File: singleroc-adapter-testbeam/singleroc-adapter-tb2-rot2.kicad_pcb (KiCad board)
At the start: 2 copper layers, 64 x 50.8 mm, 34 parts

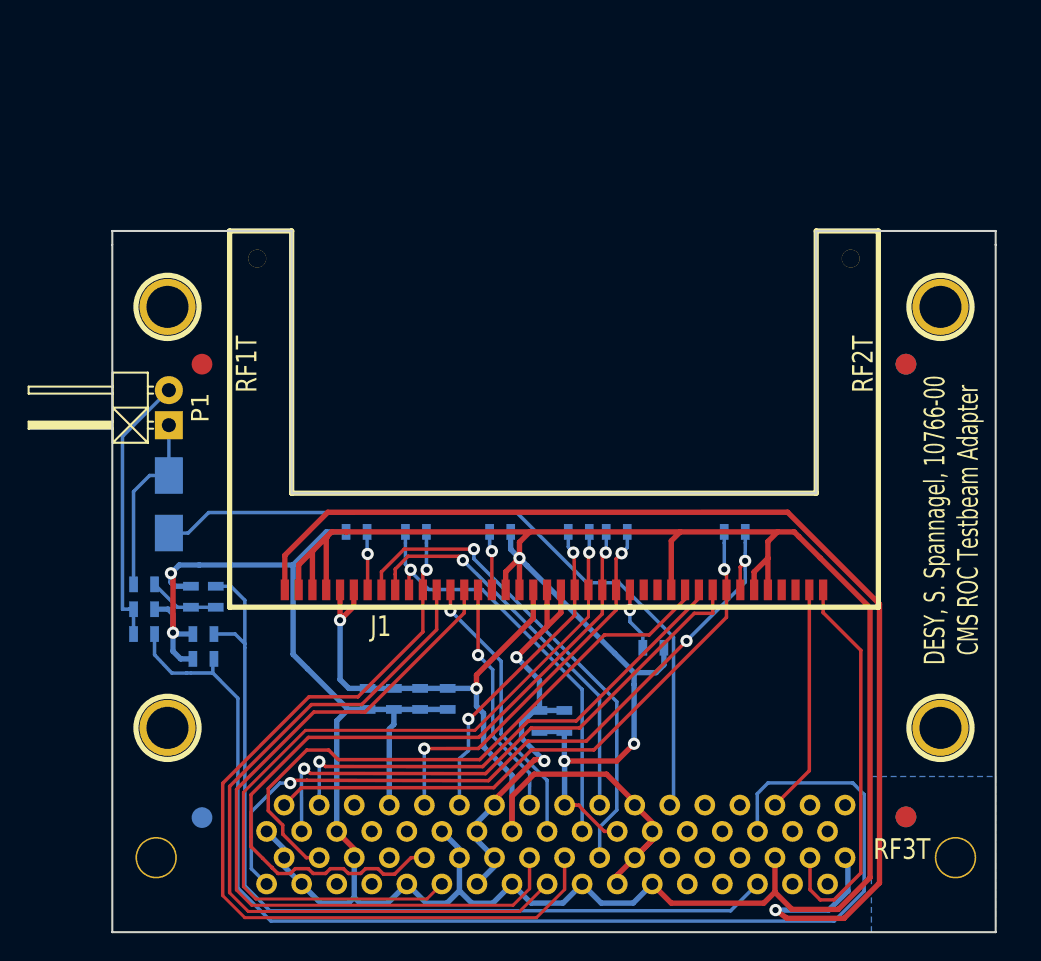
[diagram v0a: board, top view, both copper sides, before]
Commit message: Basic formfactor defined. Hispeed signals: changed resistor footprints to 0402 to save some space.
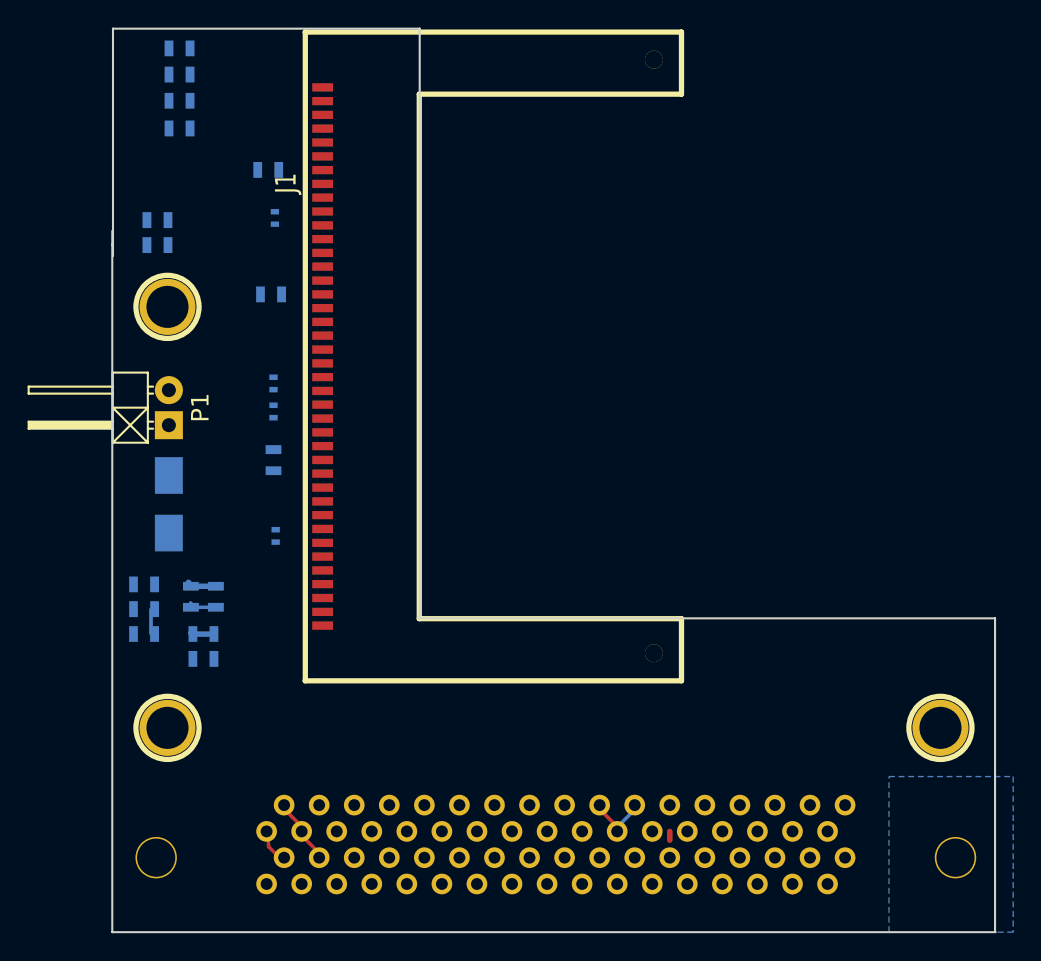
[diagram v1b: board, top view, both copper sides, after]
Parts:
- removed the ? at (147.0, 73.5)
- removed RF1B, RF1T, RF2B, RF2T, RF3B, RF3T: , Connect:1pin
- R1, R2, R3, R4: footprint SMD0603-new:SM0603 -> Resistors_SMD:R_0402
- moved C5 49.1 mm to (91.9, 54.8), turned to 180 degrees
- moved C7 47.8 mm to (91.9, 56.7), turned to 180 degrees
- moved C8 46.7 mm to (91.9, 58.6), turned to 180 degrees
- moved C9 45.7 mm to (91.9, 60.6), turned to 180 degrees
- moved C4 45.6 mm to (90.3, 67.2), turned to 180 degrees
- moved C6 45.4 mm to (90.3, 69.0), turned to 180 degrees
- moved R4 33.3 mm to (98.8, 90.1), turned to 90 degrees
- moved C3 30.7 mm to (98.7, 84.6), turned to 90 degrees
- moved C1 27.0 mm to (98.3, 63.6)
- moved R2 26.4 mm to (98.7, 81.1), turned to 90 degrees
- moved R1 24.9 mm to (98.8, 67.1), turned to 90 degrees
- moved R3 24.6 mm to (98.7, 79.0), turned to 90 degrees
- moved C2 23.9 mm to (98.5, 72.6), turned to 0 degrees
- moved J1 23.8 mm to (102.2, 77.1), turned to 270 degrees
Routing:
- net GND: track 263.5 -> 8.50 mm, vias 5 -> 0
- net AIN0: track 89.1 -> 0.00 mm
- net HV: track 87.1 -> 0.00 mm, vias 1 -> 0
- net AIN1: track 64.4 -> 0.00 mm
- net I2C_DAT+: track 63.1 -> 0.00 mm, vias 1 -> 0
- net VD: track 62.5 -> 0.00 mm, vias 2 -> 0
- net CLK+: track 58.5 -> 0.00 mm, vias 1 -> 0
- net CTR-: track 55.5 -> 0.00 mm, vias 1 -> 0
- net I2C_A2: track 55.2 -> 0.00 mm
- net I2C_A0: track 54.7 -> 0.00 mm
- net TIN+: track 54.3 -> 0.00 mm, vias 3 -> 0
- net Net-(F1-Pad2): track 53.2 -> 0.00 mm
- net SOUT-: track 44.2 -> 0.00 mm
- net TIN-: track 43.9 -> 1.48 mm, vias 1 -> 0
- net RESET: track 40.9 -> 3.06 mm, vias 1 -> 0
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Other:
- board size 64 x 50.8 mm -> 64 x 65.5 mm
- board text removed: "DESY, S. Spannagel, 10766-00 CMS ROC Testbeam Adapter"

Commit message: Proceeding...
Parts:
- C1, C10, C11, C2, C3, C4, C5, C6, C7, C8, C9, F1, R1, R2, R3, R4, R5, R6, R7, R8, R9: moved to F.Cu
- moved F1 11.9 mm to (98.1, 97.4), turned to 90 degrees
- moved R8 9.43 mm to (93.3, 86.8)
- moved R5 9.11 mm to (93.3, 89.0)
- moved C11 7.69 mm to (93.3, 91.3)
- moved R7 6.33 mm to (90.3, 87.4), turned to 270 degrees
- moved R9 2.33 mm to (90.4, 94.8), turned to 270 degrees
- moved C10 2.25 mm to (91.8, 98.5)
- moved R3 1.80 mm to (96.9, 79.1)
- moved R2 1.80 mm to (96.9, 81.1)
- moved R4 1.78 mm to (97.1, 90.0)
- moved R6 1.77 mm to (92.8, 94.8), turned to 90 degrees
- moved C3 1.41 mm to (97.5, 83.8), turned to 0 degrees
- moved C5 1.40 mm to (91.0, 55.9)
- moved C7 1.40 mm to (91.0, 57.8)
- moved C8 1.40 mm to (91.0, 59.7)
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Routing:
- net HV: track 0.00 -> 98.3 mm, vias 0 -> 1
- net TOUT-: track 0.00 -> 70.1 mm, vias 0 -> 1
- net I2C_DAT+: track 0.00 -> 69.6 mm, vias 0 -> 1
- net GND: track 8.50 -> 77.2 mm, vias 0 -> 18
- net I2C_DAT-: track 0.00 -> 67.6 mm, vias 0 -> 1
- net VD: track 0.00 -> 67.5 mm, vias 0 -> 7
- net I2C_A0: track 0.00 -> 62.0 mm
- net TOUT+: track 2.91 -> 64.8 mm, vias 0 -> 1
- net VA: track 0.00 -> 61.8 mm, vias 0 -> 4
- net I2C_A1: track 0.00 -> 54.1 mm
- net CLK+: track 0.00 -> 52.2 mm, vias 0 -> 2
- net I2C_A2: track 0.00 -> 51.8 mm
- net CLK-: track 0.00 -> 46.6 mm, vias 0 -> 1
- net I2C_A3: track 0.00 -> 46.1 mm
- net CTR-: track 0.00 -> 45.9 mm, vias 0 -> 1
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- added copper zone on In2.Cu, net GND
- added copper zone on In1.Cu, net VA
- added copper zone on In1.Cu, net VD
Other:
- copper layers 2 -> 4

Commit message: Recovery from KiCAD crash
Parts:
- moved F1 38.3 mm to (136.0, 103.4), turned to 180 degrees
- moved R7 11.0 mm to (91.1, 98.3), turned to 0 degrees
- moved C10 6.36 mm to (96.8, 102.4), turned to 270 degrees
- moved R9 5.48 mm to (94.4, 98.6)
- moved R6 5.41 mm to (96.7, 98.6)
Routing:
- net RTD+: track 4.84 -> 112.7 mm
- net AIN0: track 2.33 -> 72.2 mm
- net AIN1: track 3.02 -> 60.8 mm
- net Net-(F1-Pad2): track 0.00 -> 9.09 mm
- net GND: track 77.2 -> 72.6 mm, vias 18 -> 16
- net Net-(R6-Pad2): track 8.37 -> 5.02 mm

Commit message: First draft, everything should be connected.
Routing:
- net AIN2: track 0.00 -> 86.3 mm, vias 0 -> 1
- net Net-(J1-Pad1): track 0.00 -> 85.4 mm, vias 0 -> 1
- net RESET: track 0.65 -> 26.9 mm
- net GND: track 72.6 -> 80.0 mm, vias 16 -> 19
- net Net-(C3-Pad2): track 0.00 -> 4.63 mm
- net Net-(C2-Pad2): track 0.00 -> 3.62 mm
- net AIN0: track 72.2 -> 70.2 mm, vias 0 -> 1
